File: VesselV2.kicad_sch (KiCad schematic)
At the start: 222 parts, among them J1 USB_B_Mini, SW1 SW_Push, U1 ATmega32U4-A, Y1 16MHz

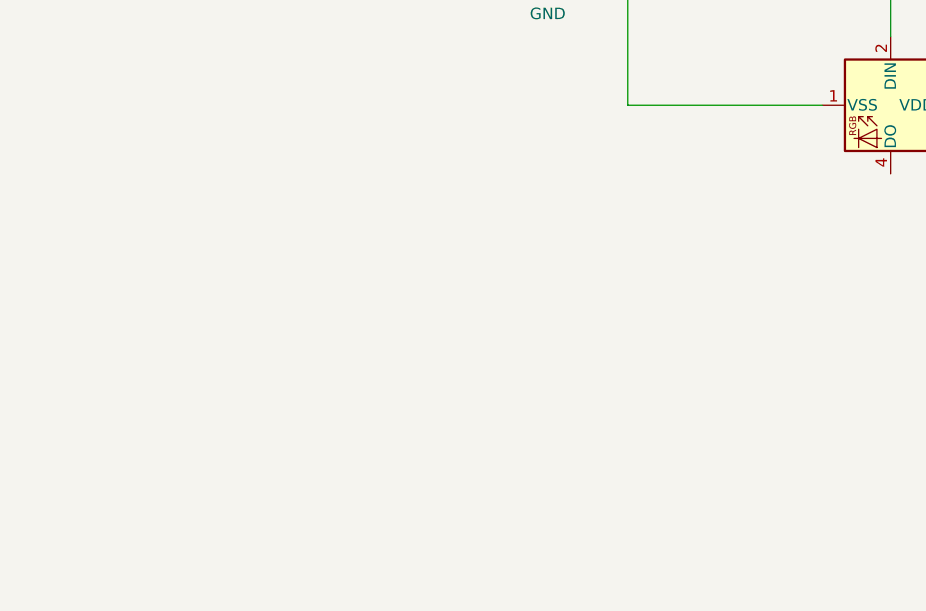
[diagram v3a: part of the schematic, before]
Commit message: Grid origin set- Prep for Freecad case design
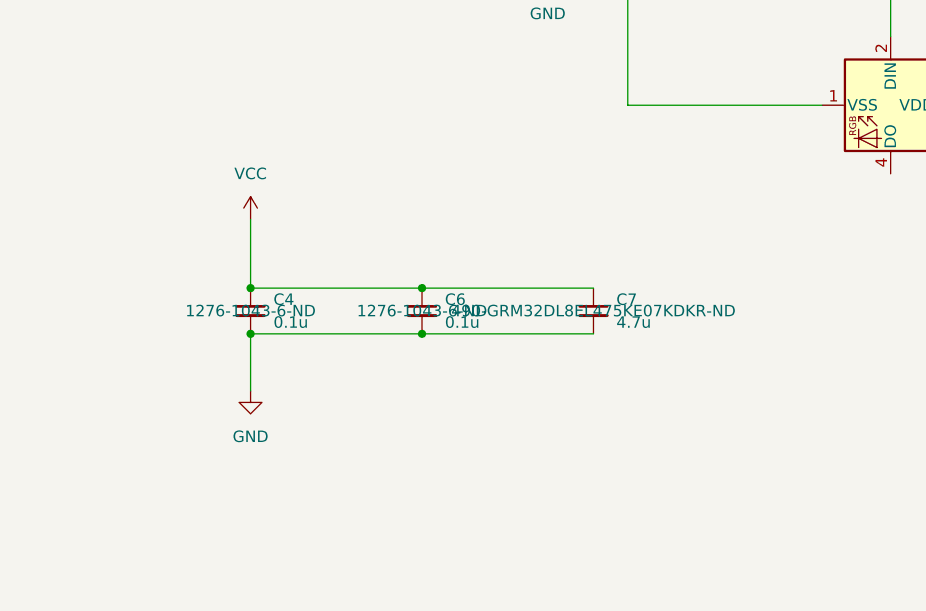
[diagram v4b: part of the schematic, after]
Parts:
- added C4, C6: 0.1u, Capacitor_SMD:C_0805_2012Metric_Pad1.18x1.45mm_HandSolder, symbol Device:C_Small
- added C7: 4.7u, Capacitor_SMD:C_0805_2012Metric_Pad1.18x1.45mm_HandSolder, symbol Device:C_Small
- D103: DigikeyPartNumber (none) -> 1830-1106-6-ND; ManufacturerPartNumber (none) -> IN-PI554FCH; MouserPartNumber (none) -> 743-IN-PI554FCH
- F2: ManufacturerPartNumber (none) -> 3413.0113.22; MouserPartNumber 693-3413.0113.22 -> 693-3413.0113.22
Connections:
- net GND: now also C4.2, C6.2, C7.2
- net VCC: now also C4.1, C6.1, C7.1
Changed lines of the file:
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@@
   (junction (at 123.19 127) (diameter 0) (color 0 0 0 0)
   )
+  (junction (at 336.55 193.04) (diameter 0) (color 0 0 0 0)
+  )
   (junction (at 342.9 68.58) (diameter 0) (color 0 0 0 0)
   )
@@
   (junction (at 125.73 170.18) (diameter 0) (color 0 0 0 0)
   )
+  (junction (at 317.5 193.04) (diameter 0) (color 0 0 0 0)
+  )
   (junction (at 307.34 87.63) (diameter 0) (color 0 0 0 0)
   )
@@
   (junction (at 176.53 147.32) (diameter 0) (color 0 0 0 0)
   )
+  (junction (at 336.55 187.96) (diameter 0) (color 0 0 0 0)
+  )
   (junction (at 217.17 153.67) (diameter 0) (color 0 0 0 0)
   )
@@
   (junction (at 171.45 137.16) (diameter 0) (color 0 0 0 0)
   )
+  (junction (at 317.5 187.96) (diameter 0) (color 0 0 0 0)
+  )
   (junction (at 107.95 198.12) (diameter 0) (color 0 0 0 0)
   )
@@
     (stroke (width 0) (type default))
   )
+  (wire (pts (xy 317.5 193.04) (xy 317.5 199.39))
+    (stroke (width 0) (type default))
+  )
   (wire (pts (xy 118.11 111.76) (xy 109.22 111.76))
     (stroke (width 0) (type default))
@@
     (stroke (width 0) (type default))
   )
+  (wire (pts (xy 336.55 187.96) (xy 317.5 187.96))
+    (stroke (width 0) (type default))
+  )
   (wire (pts (xy 91.44 187.96) (xy 91.44 204.47))
     (stroke (width 0) (type default))
@@
     (stroke (width 0) (type default))
   )
+  (wire (pts (xy 355.6 187.96) (xy 336.55 187.96))
+    (stroke (width 0) (type default))
+  )
   (wire (pts (xy 138.43 107.95) (xy 149.86 107.95))
     (stroke (width 0) (type default))
@@
     (stroke (width 0) (type default))
   )
+  (wire (pts (xy 317.5 187.96) (xy 317.5 180.34))
+    (stroke (width 0) (type default))
+  )
   (wire (pts (xy 130.81 198.12) (xy 142.24 198.12))
     (stroke (width 0) (type default))
@@
     (stroke (width 0) (type default))
   )
+  (wire (pts (xy 336.55 193.04) (xy 317.5 193.04))
+    (stroke (width 0) (type default))
+  )
   (wire (pts (xy 205.74 111.76) (xy 205.74 116.84))
     (stroke (width 0) (type default))
@@
     (stroke (width 0) (type default))
   )
+  (wire (pts (xy 355.6 193.04) (xy 336.55 193.04))
+    (stroke (width 0) (type default))
+  )
   (wire (pts (xy 134.62 127) (xy 149.86 127))
     (stroke (width 0) (type default))
@@
     )
   )
+  (symbol (lib_id "power:VCC") (at 317.5 180.34 0) (unit 1)
+    (in_bom yes) (on_board yes) (dnp no) (fields_autoplaced)
+    (property "Reference" "#PWR01" (at 317.5 184.15 0)
+      (effects (font (size 1.27 1.27)) hide)
+    )
+    (property "Value" "VCC" (at 317.5 175.26 0)
+      (effects (font (size 1.27 1.27)))
+    )
+    (property "Footprint" "" (at 317.5 180.34 0)
+      (effects (font (size 1.27 1.27)) hide)
+    )
+    (property "Datasheet" "" (at 317.5 180.34 0)
+      (effects (font (size 1.27 1.27)) hide)
+    )
+    (pin "1")
+    (instances
+      (project "VesselV2"
+        (path "/c445c6d8-4fde-4143-815a-ac483f9e4cc3"
+          (reference "#PWR01") (unit 1)
+        )
+      )
+    )
+  )
   (symbol (lib_id "PCM_marbastlib-mx:MX_SW_solder") (at 147.32 100.33 0) (unit 1)
     (in_bom yes) (on_board yes) (dnp no) (fields_autoplaced)
@@
       (effects (font (size 1.27 1.27)))
     )
-    (property "ManufacturerPartNumber" "" (at 251.46 34.29 0)
+    (property "ManufacturerPartNumber" "3413.0113.22" (at 251.46 34.29 0)
       (effects (font (size 1.27 1.27)) hide)
     )
-    (property "MouserPartNumber" "693-3413.0113.22 " (at 251.46 34.29 0)
+    (property "MouserPartNumber" "693-3413.0113.22" (at 251.46 34.29 0)
       (effects (font (size 1.27 1.27)) hide)
     )
@@
     )
   )
+  (symbol (lib_id "Device:C_Small") (at 317.5 190.5 0) (unit 1)
+    (in_bom yes) (on_board yes) (dnp no) (fields_autoplaced)
+    (property "Reference" "C4" (at 320.04 189.2363 0)
+      (effects (font (size 1.27 1.27)) (justify left))
+    )
+    (property "Value" "0.1u" (at 320.04 191.7763 0)
+      (effects (font (size 1.27 1.27)) (justify left))
+    )
+    (property "Footprint" "Capacitor_SMD:C_0805_2012Metric_Pad1.18x1.45mm_HandSolder" (at 317.5 190.5 0)
+      (effects (font (size 1.27 1.27)) hide)
+    )
+    (property "Datasheet" "https://mm.digikey.com/Volume0/opasdata/d220001/medias/docus/503/CL05A104KA5NNNC.pdf" (at 317.5 190.5 0)
+      (effects (font (size 1.27 1.27)) hide)
+    )
+    (property "DigikeyPartNumber" "1276-1043-6-ND" (at 317.5 190.5 0)
+      (effects (font (size 1.27 1.27)))
+    )
+    (property "ManufacturerPartNumber" "CL05A104KA5NNNC" (at 317.5 190.5 0)
+      (effects (font (size 1.27 1.27)) hide)
+    )
+    (property "MouserPartNumber" "187-CL05A104KA5NNNC" (at 317.5 190.5 0)
+      (effects (font (size 1.27 1.27)) hide)
+    )
+    (pin "1")
+    (pin "2")
+    (instances
+      (project "VesselV2"
+        (path "/c445c6d8-4fde-4143-815a-ac483f9e4cc3"
+          (reference "C4") (unit 1)
+        )
+      )
+    )
+  )
   (symbol (lib_id "Device:D_Small") (at 210.82 177.8 90) (unit 1)
     (in_bom yes) (on_board yes) (dnp no) (fields_autoplaced)
@@
       (effects (font (size 1.27 1.27)) (justify left top) hide)
     )
+    (property "DigikeyPartNumber" "1830-1106-6-ND" (at 388.62 167.64 0)
+      (effects (font (size 1.27 1.27)) hide)
+    )
+    (property "ManufacturerPartNumber" "IN-PI554FCH" (at 388.62 167.64 0)
+      (effects (font (size 1.27 1.27)) hide)
+    )
+    (property "MouserPartNumber" "743-IN-PI554FCH" (at 388.62 167.64 0)
+      (effects (font (size 1.27 1.27)) hide)
+    )
     (pin "1")
     (pin "2")
@@
     )
   )
+  (symbol (lib_id "Device:C_Small") (at 355.6 190.5 0) (unit 1)
+    (in_bom yes) (on_board yes) (dnp no) (fields_autoplaced)
+    (property "Reference" "C7" (at 358.14 189.2363 0)
+      (effects (font (size 1.27 1.27)) (justify left))
+    )
+    (property "Value" "4.7u" (at 358.14 191.7763 0)
+      (effects (font (size 1.27 1.27)) (justify left))
+    )
+    (property "Footprint" "Capacitor_SMD:C_0805_2012Metric_Pad1.18x1.45mm_HandSolder" (at 355.6 190.5 0)
+      (effects (font (size 1.27 1.27)) hide)
+    )
+    (property "Datasheet" "https://search.murata.co.jp/Ceramy/image/img/A01X/G101/ENG/GRM32DL8EL475KE07-01A.pdf" (at 355.6 190.5 0)
+      (effects (font (size 1.27 1.27)) hide)
+    )
+    (property "DigikeyPartNumber" "490-GRM32DL8EL475KE07KDKR-ND" (at 355.6 190.5 0)
+      (effects (font (size 1.27 1.27)))
+    )
+    (property "ManufacturerPartNumber" "GRM32DL8EL475KE07K" (at 355.6 190.5 0)
+      (effects (font (size 1.27 1.27)) hide)
+    )
+    (property "MouserPartNumber" "81-GRM3DL8EL475KE07K" (at 355.6 190.5 0)
+      (effects (font (size 1.27 1.27)) hide)
+    )
+    (pin "1")
+    (pin "2")
+    (instances
+      (project "VesselV2"
+        (path "/c445c6d8-4fde-4143-815a-ac483f9e4cc3"
+          (reference "C7") (unit 1)
+        )
+      )
+    )
+  )
   (symbol (lib_id "Device:D_Small") (at 222.25 144.78 90) (unit 1)
     (in_bom yes) (on_board yes) (dnp no) (fields_autoplaced)
@@
     )
   )
+  (symbol (lib_id "power:GND") (at 317.5 199.39 0) (unit 1)
+    (in_bom yes) (on_board yes) (dnp no) (fields_autoplaced)
+    (property "Reference" "#PWR02" (at 317.5 205.74 0)
+      (effects (font (size 1.27 1.27)) hide)
+    )
+    (property "Value" "GND" (at 317.5 204.47 0)
+      (effects (font (size 1.27 1.27)))
+    )
+    (property "Footprint" "" (at 317.5 199.39 0)
+      (effects (font (size 1.27 1.27)) hide)
+    )
+    (property "Datasheet" "" (at 317.5 199.39 0)
+      (effects (font (size 1.27 1.27)) hide)
+    )
+    (pin "1")
+    (instances
+      (project "VesselV2"
+        (path "/c445c6d8-4fde-4143-815a-ac483f9e4cc3"
+          (reference "#PWR02") (unit 1)
+        )
+      )
+    )
+  )
   (symbol (lib_id "PCM_marbastlib-mx:MX_SW_solder") (at 208.28 119.38 0) (unit 1)
     (in_bom yes) (on_board yes) (dnp no) (fields_autoplaced)
@@
         )
       )
+    )
+  )
+  (symbol (lib_id "Device:C_Small") (at 336.55 190.5 0) (unit 1)
+    (in_bom yes) (on_board yes) (dnp no) (fields_autoplaced)
+    (property "Reference" "C6" (at 339.09 189.2363 0)
+      (effects (font (size 1.27 1.27)) (justify left))
+    )
+    (property "Value" "0.1u" (at 339.09 191.7763 0)
+      (effects (font (size 1.27 1.27)) (justify left))
+    )
+    (property "Footprint" "Capacitor_SMD:C_0805_2012Metric_Pad1.18x1.45mm_HandSolder" (at 336.55 190.5 0)
+      (effects (font (size 1.27 1.27)) hide)
+    )
+    (property "Datasheet" "https://mm.digikey.com/Volume0/opasdata/d220001/medias/docus/503/CL05A104KA5NNNC.pdf" (at 336.55 190.5 0)
+      (effects (font (size 1.27 1.27)) hide)
+    )
+    (property "DigikeyPartNumber" "1276-1043-6-ND" (at 336.55 190.5 0)
+      (effects (font (size 1.27 1.27)))
+    )
+    (property "ManufacturerPartNumber" "CL05A104KA5NNNC" (at 336.55 190.5 0)
+      (effects (font (size 1.27 1.27)) hide)
+    )
+    (property "MouserPartNumber" "187-CL05A104KA5NNNC" (at 336.55 190.5 0)
+      (effects (font (size 1.27 1.27)) hide)
+    )
+    (pin "1")
+    (pin "2")
+    (instances
+      (project "VesselV2"
+        (path "/c445c6d8-4fde-4143-815a-ac483f9e4cc3"
+          (reference "C6") (unit 1)
+        )
+      )
